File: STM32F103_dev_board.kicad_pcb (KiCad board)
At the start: 4 copper layers, 39.4 x 83.8 mm, 40 parts, among them IC2 FT232RNL-REEL, J1 Conn_ARM_JTAG_SWD_20, J2 Conn_01x20_Pin, J3 Conn_01x20_Pin, J6 USB4800-03-A, U1 STM32F103RBTx, Y1 8MHz, Y2 Crystal_GND23

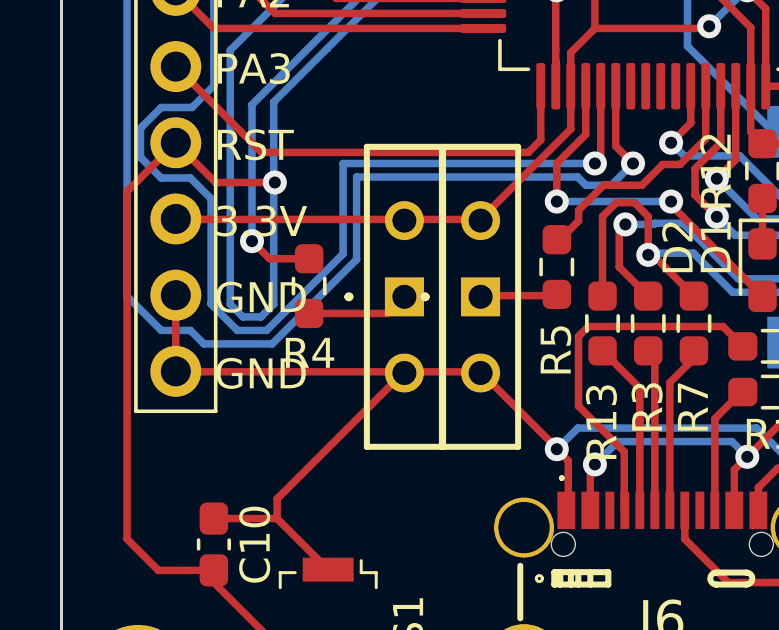
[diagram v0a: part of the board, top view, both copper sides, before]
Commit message: Moved R4 resistor position slightly
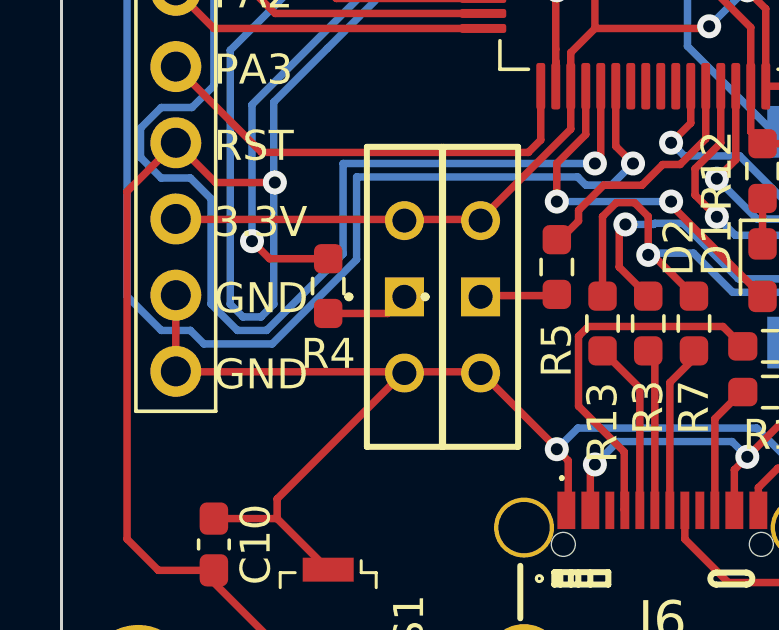
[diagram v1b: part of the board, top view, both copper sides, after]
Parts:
- moved R4 0.63 mm to (134.6, 126.0)
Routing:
- net Net-(S2-COM): track 3.40 -> 2.77 mm
- net BOOT0: track 26.2 -> 26.8 mm
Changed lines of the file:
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@@
   )
   (footprint "Resistor_SMD:R_0603_1608Metric_Pad0.98x0.95mm_HandSolder" (layer "F.Cu")
-    (at 133.985 126.0075 90)
+    (at 134.62 126.0075 90)
     (descr "Resistor SMD 0603 (1608 Metric), square (rectangular) end terminal, IPC_7351 nominal with elongated pad for handsoldering. (Body size source: IPC-SM-782 page 72, https://www.pcb-3d.com/wordpress/wp-content/uploads/ipc-sm-782a_amendment_1_and_2.pdf), generated with kicad-footprint-generator")
     (tags "resistor handsolder")
@@
   (segment (start 151.13 116.42) (end 161.02 116.42) (width 0.25) (layer "F.Cu") (net 41))
   (segment (start 161.02 116.42) (end 161.29 116.15) (width 0.25) (layer "F.Cu") (net 41))
-  (segment (start 133.985 126.92) (end 136.605 126.92) (width 0.25) (layer "F.Cu") (net 42))
+  (segment (start 134.62 126.92) (end 136.605 126.92) (width 0.25) (layer "F.Cu") (net 42))
   (segment (start 136.605 126.92) (end 137.16 126.365) (width 0.25) (layer "F.Cu") (net 42))
   (segment (start 144.488 133.462) (end 144.508 133.482) (width 0.25) (layer "F.Cu") (net 43))
@@
   (segment (start 161.776701 122.595) (end 162.465 123.283299) (width 0.25) (layer "B.Cu") (net 53))
   (segment (start 160.803299 122.595) (end 161.776701 122.595) (width 0.25) (layer "B.Cu") (net 53))
+  (segment (start 134.62 125.095) (end 132.6655 125.095) (width 0.25) (layer "F.Cu") (net 54))
   (segment (start 143.705 109.605) (end 143.51 109.8) (width 0.25) (layer "F.Cu") (net 54))
-  (segment (start 132.6655 125.095) (end 133.985 125.095) (width 0.25) (layer "F.Cu") (net 54))
   (segment (start 132.6655 125.095) (end 132.08 124.5095) (width 0.25) (layer "F.Cu") (net 54))
   (segment (start 143.705 107.995) (end 143.705 109.605) (width 0.25) (layer "F.Cu") (net 54))

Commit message: Minor changes
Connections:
- S2 pad 3: unconnected-(S2-NC-Pad3) -> VCC3V3
- S3 pad 3: unconnected-(S3-NC-Pad3) -> VCC3V3
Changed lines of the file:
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@@
   (net 89 "PB5")
   (net 90 "Net-(S3-COM)")
-  (net 91 "unconnected-(S2-NC-Pad3)")
-  (net 92 "unconnected-(S3-NC-Pad3)")
   (footprint "Capacitor_SMD:C_0603_1608Metric_Pad1.08x0.95mm_HandSolder" (layer "F.Cu")
     (at 152.72 130.12 180)
@@
       (net 78 "GND") (pinfunction "NO") (pintype "passive"))
     (pad "3" thru_hole circle (at -2.54 0 270) (size 1.3 1.3) (drill 0.8) (layers "*.Cu" "*.Mask")
-      (net 91 "unconnected-(S2-NC-Pad3)") (pinfunction "NC") (pintype "no_connect"))
-    (model "C:\\Lib\\SamacSys_Parts\\SamacSys_Parts.3dshapes\\BSI-10.stp"
+      (net 80 "VCC3V3") (pinfunction "NC") (pintype "passive"))
+    (model "C:\\lib\\samacsys\\SamacSys_Parts.3dshapes\\BSI-10.stp"
       (offset (xyz 0 0 0))
       (scale (xyz 1 1 1))
@@
     (pad "5" smd rect (at 1.25 -0.95 180) (size 0.6 1.2) (layers "F.Cu" "F.Paste" "F.Mask")
       (net 80 "VCC3V3") (pinfunction "OUT") (pintype "output"))
-    (model "C:\\Lib\\SamacSys_Parts\\SamacSys_Parts.3dshapes\\TLV75733PDBVR.stp"
+    (model "C:\\lib\\samacsys\\SamacSys_Parts.3dshapes\\TLV75733PDBVR.stp"
       (offset (xyz 0 0 0))
       (scale (xyz 1 1 1))
@@
       (net 78 "GND") (pinfunction "NO") (pintype "passive"))
     (pad "3" thru_hole circle (at -2.54 0 270) (size 1.3 1.3) (drill 0.8) (layers "*.Cu" "*.Mask")
-      (net 92 "unconnected-(S3-NC-Pad3)") (pinfunction "NC") (pintype "no_connect"))
-    (model "C:\\Lib\\SamacSys_Parts\\SamacSys_Parts.3dshapes\\BSI-10.stp"
+      (net 80 "VCC3V3") (pinfunction "NC") (pintype "passive"))
+    (model "C:\\lib\\samacsys\\SamacSys_Parts.3dshapes\\BSI-10.stp"
       (offset (xyz 0 0 0))
       (scale (xyz 1 1 1))
@@
     (pad "28" smd rect (at 3.512 4.225 180) (size 0.45 1.725) (layers "B.Cu" "B.Paste" "B.Mask")
       (net 76 "unconnected-(IC2-OSCO-Pad28)") (pinfunction "OSCO") (pintype "passive+no_connect"))
-    (model "C:\\Lib\\SamacSys_Parts\\SamacSys_Parts.3dshapes\\FT232RNL-TUBE.stp"
-      (offset (xyz 0 0 0))
-      (scale (xyz 1 1 1))
+    (model "C:\\lib\\samacsys\\SamacSys_Parts.3dshapes\\FT232RNL-REEL.stp"
+      (offset (xyz 0 0 0))
+      (scale (xyz 1 1 1))

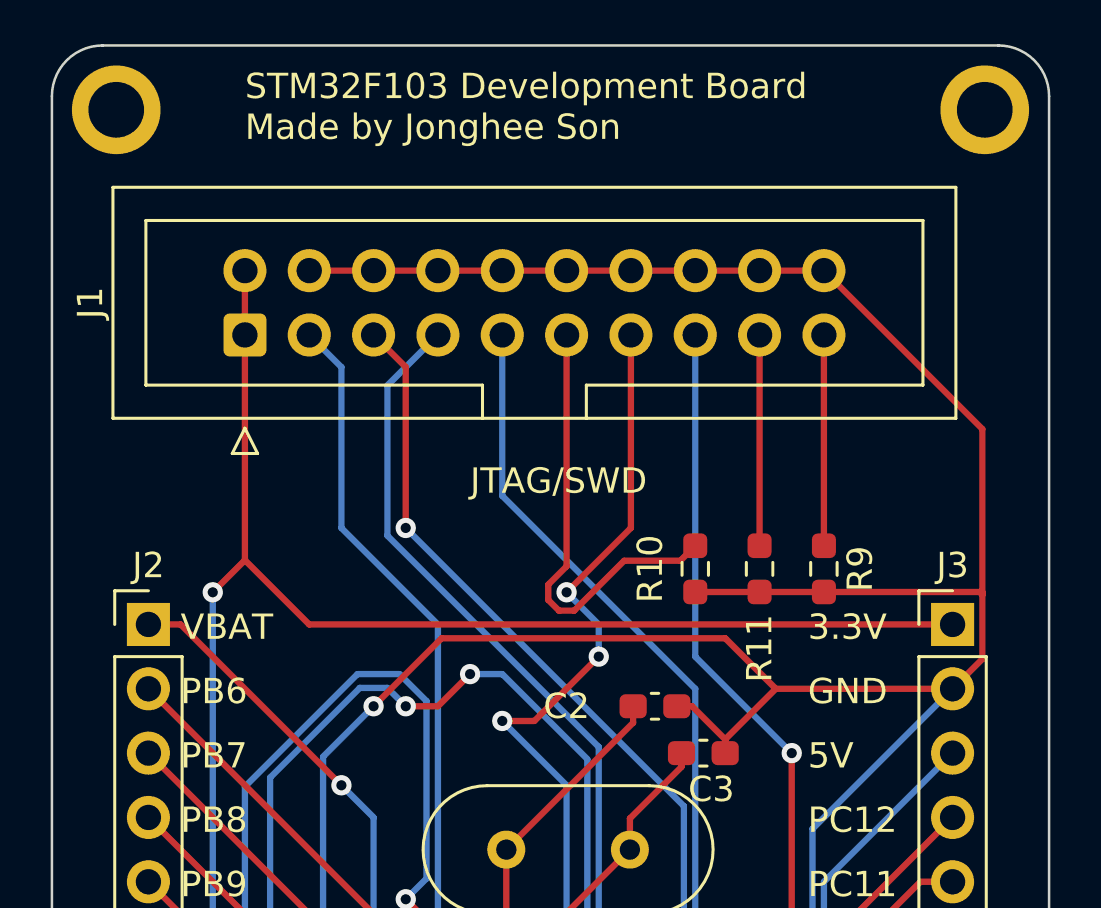
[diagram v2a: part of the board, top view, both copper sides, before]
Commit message: Changed direction of JTAG connector for easy connection
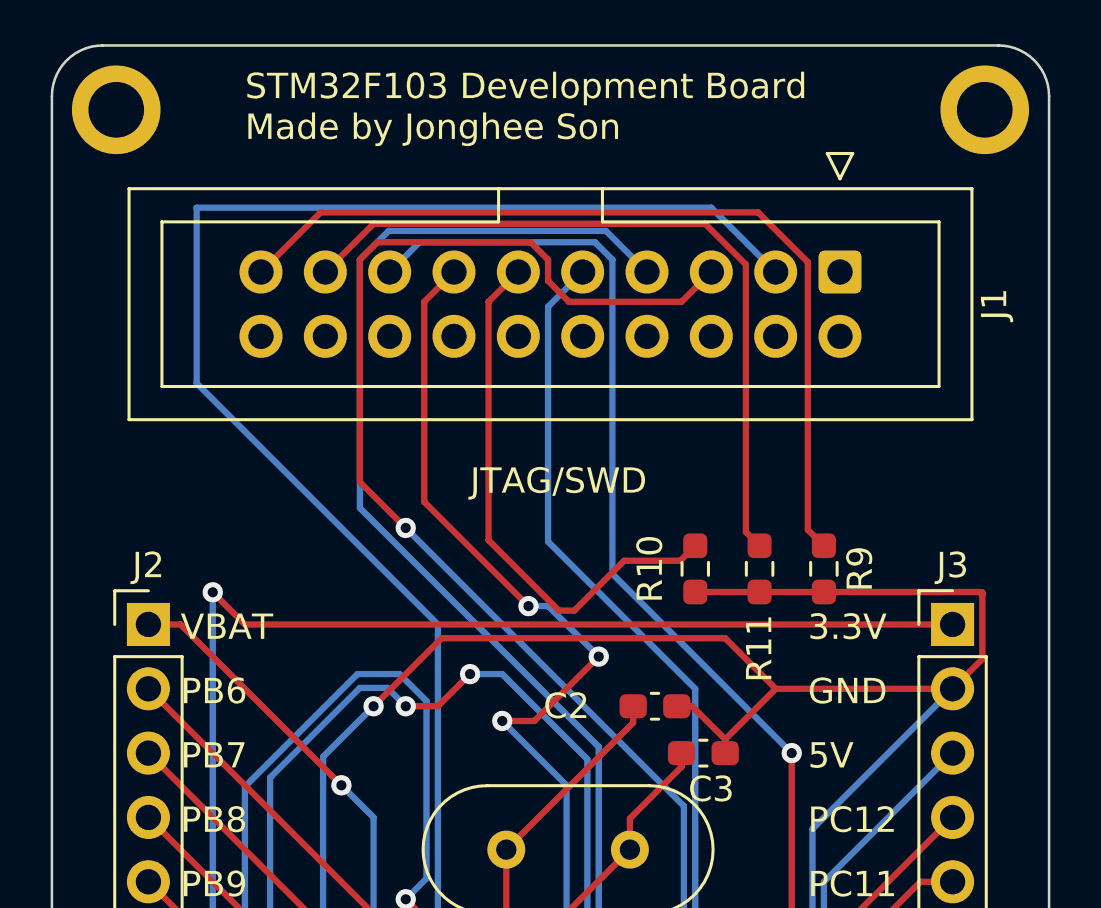
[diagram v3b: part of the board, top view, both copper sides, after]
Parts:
- moved J1 23.6 mm to (156.8, 66.7), turned to -90 degrees
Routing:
- net GND: track 306.2 -> 270.6 mm
- net JNTRST: track 42.9 -> 73.7 mm
- net Net-(J1-DBGACK/NC): track 8.32 -> 34.8 mm
- net Net-(J1-DBGRQ/NC): track 8.32 -> 29.4 mm
- net JTDI: track 44.7 -> 64.0 mm
- net JTMS/SWDIO: track 52.7 -> 67.8 mm
- net RESET: track 122.5 -> 136.4 mm
- net VCC3V3: track 147.3 -> 134.8 mm
- net JTDO: track 43.9 -> 48.6 mm
- net Net-(J1-RTCK): track 17.8 -> 21.4 mm
- net JTCK/SWCLK: track 42.8 -> 45.1 mm

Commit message: Added copper pour for 1st & 2nd layer
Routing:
- net VCC3V3: track 134.8 -> 66.4 mm, vias 5 -> 4
- added copper zone on B.Cu, net GND
- added copper zone on F.Cu, net GND
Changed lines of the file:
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@@
   (title_block
     (title "STM32F103RBT6 Dev Board")
-    (date "2023-12-15")
-    (rev "1.2.2")
+    (date "2023-12-16")
+    (rev "1.2.3")
   )
   (layers
@@
   (segment (start 150.43 109.22) (end 145.36 109.22) (width 0.25) (layer "F.Cu") (net 80))
   (segment (start 143.281695 110.769695) (end 143.51 110.998) (width 0.25) (layer "F.Cu") (net 80))
-  (segment (start 161.29 80.59) (end 133.35 80.59) (width 0.25) (layer "F.Cu") (net 80))
   (segment (start 152.405 124.841) (end 152.405 122.52) (width 0.25) (layer "F.Cu") (net 80))
   (segment (start 143.51 117.42) (end 143.51 113.030685) (width 0.25) (layer "F.Cu") (net 80))
   (segment (start 142.705 120.775) (end 139.695 123.785) (width 0.25) (layer "F.Cu") (net 80))
   (segment (start 142.705 118.225) (end 143.51 117.42) (width 0.25) (layer "F.Cu") (net 80))
-  (segment (start 133.35 80.59) (end 132.08 79.32) (width 0.25) (layer "F.Cu") (net 80))
   (segment (start 141.705 109.955) (end 142.095 110.345) (width 0.25) (layer "F.Cu") (net 80))
   (segment (start 143.51 114.88) (end 142.484695 114.88) (width 0.25) (layer "F.Cu") (net 80))
@@
   (segment (start 149.205 119.345) (end 150.911 119.345) (width 0.25) (layer "F.Cu") (net 80))
   (segment (start 149.205 116.765) (end 148.59 116.15) (width 0.25) (layer "F.Cu") (net 80))
-  (segment (start 132.08 79.32) (end 132.08 79.32) (width 0.25) (layer "F.Cu") (net 80))
   (segment (start 137.155 123.785) (end 129.555 123.785) (width 0.25) (layer "F.Cu") (net 80))
   (segment (start 151.13 109.92) (end 150.43 109.22) (width 0.25) (layer "F.Cu") (net 80))
@@
   (via (at 147.32 117.348) (size 0.8) (drill 0.4) (layers "F.Cu" "B.Cu") (net 80))
   (via (at 151.257 118.999) (size 0.8) (drill 0.4) (layers "F.Cu" "B.Cu") (net 80))
-  (via (at 132.08 79.32) (size 0.8) (drill 0.4) (layers "F.Cu" "B.Cu") (net 80))
   (via (at 143.51 110.998) (size 0.8) (drill 0.4) (layers "F.Cu" "B.Cu") (net 80))
   (segment (start 148.59 116.15) (end 148.518 116.15) (width 0.25) (layer "B.Cu") (net 80))
   (segment (start 147.32 117.42) (end 147.32 117.348) (width 0.25) (layer "B.Cu") (net 80))
   (segment (start 147.32 117.348) (end 147.392 117.348) (width 0.25) (layer "B.Cu") (net 80))
-  (segment (start 141.695 111.795) (end 132.08 102.18) (width 0.25) (layer "B.Cu") (net 80))
-  (segment (start 142.785 111.723) (end 143.51 110.998) (width 0.25) (layer "B.Cu") (net 80))
-  (segment (start 142.785 111.795) (end 141.695 111.795) (width 0.25) (layer "B.Cu") (net 80))
-  (segment (start 132.08 102.18) (end 132.08 79.32) (width 0.25) (layer "B.Cu") (net 80))
   (segment (start 147.32 117.42) (end 147.32 117.42) (width 0.25) (layer "B.Cu") (net 80))
   (segment (start 151.257 118.999) (end 151.42825 119.17025) (width 0.25) (layer "B.Cu") (net 80))
   (segment (start 148.518 116.15) (end 147.32 117.348) (width 0.25) (layer "B.Cu") (net 80))
   (segment (start 151.42825 119.17025) (end 151.42825 120.865) (width 0.25) (layer "B.Cu") (net 80))
-  (segment (start 142.785 111.795) (end 142.785 111.723) (width 0.25) (layer "B.Cu") (net 80))
   (segment (start 130.81 80.59) (end 129.54 80.59) (width 0.25) (layer "F.Cu") (net 81))
   (segment (start 138.43 107.26) (end 138.43 108.57) (width 0.25) (layer "F.Cu") (net 81))
@@
   (segment (start 139.71 126.31) (end 139.695 126.325) (width 0.25) (layer "F.Cu") (net 90))
   (segment (start 142.1765 126.325) (end 139.695 126.325) (width 0.25) (layer "F.Cu") (net 90))
+  (zone (net 78) (net_name "GND") (layer "F.Cu") (hatch edge 0.5)
+    (priority 2)
+    (connect_pads (clearance 0.5))
+    (min_thickness 0.25) (filled_areas_thickness no)
+    (fill yes (thermal_gap 0.5) (thermal_bridge_width 0.5))
+    (polygon
+      (pts
+        (xy 125.73 57.15)
+        (xy 165.1 57.15)
+        (xy 165.1 141.605)
+        (xy 125.73 141.605)
+      )
+    )
+  )
   (zone (net 80) (net_name "VCC3V3") (layer "In1.Cu") (hatch edge 0.5)
     (connect_pads (clearance 0.5))
@@
     (connect_pads (clearance 0.5))
     (min_thickness 0.25) (filled_areas_thickness no)
+    (fill yes (thermal_gap 0.5) (thermal_bridge_width 0.5))
+    (polygon
+      (pts
+        (xy 125.73 57.15)
+        (xy 165.1 57.15)
+        (xy 165.1 141.605)
+        (xy 125.73 141.605)
+      )
+    )
+  )
+  (zone (net 78) (net_name "GND") (layer "B.Cu") (hatch edge 0.5)
+    (priority 3)
+    (connect_pads (clearance 0.5))
+    (min_thickness 0.25) (filled_areas_thickness no)

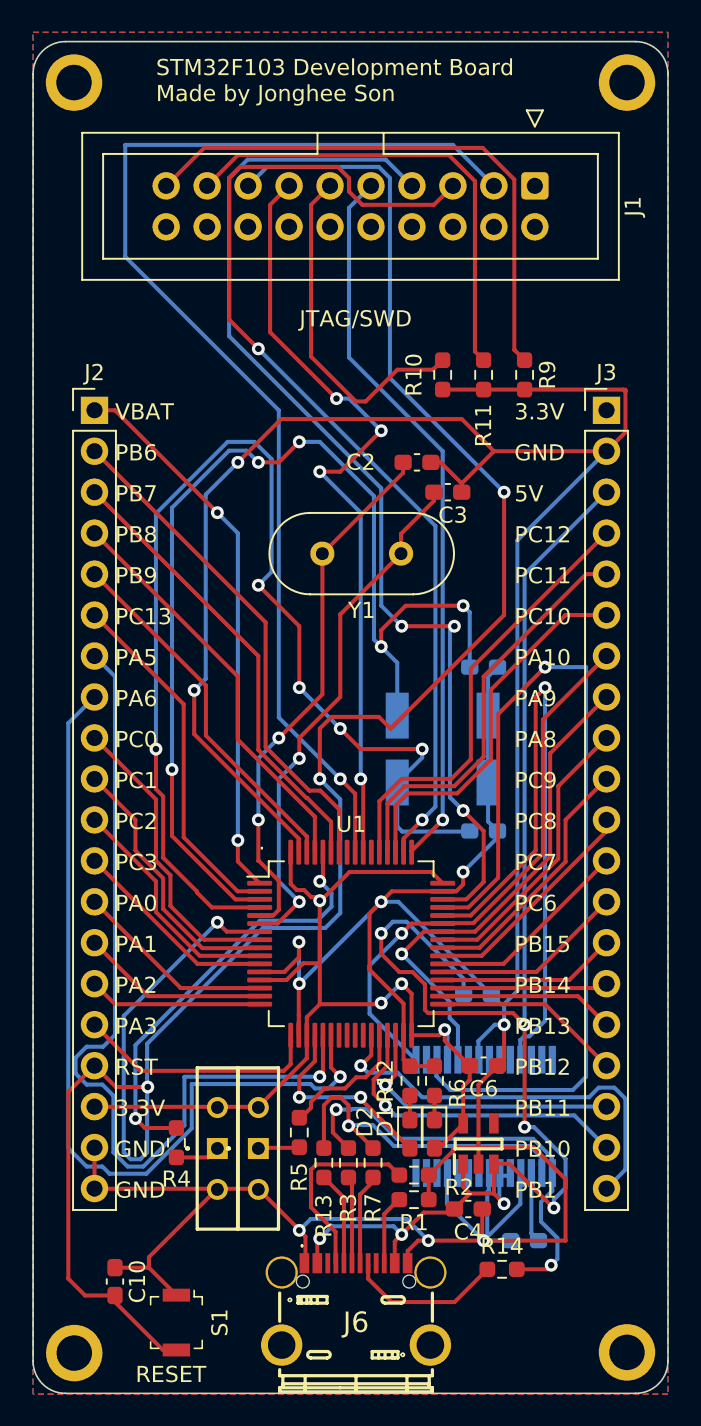
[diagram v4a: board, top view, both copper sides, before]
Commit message: Changed 8MHz oscillator to SMD one
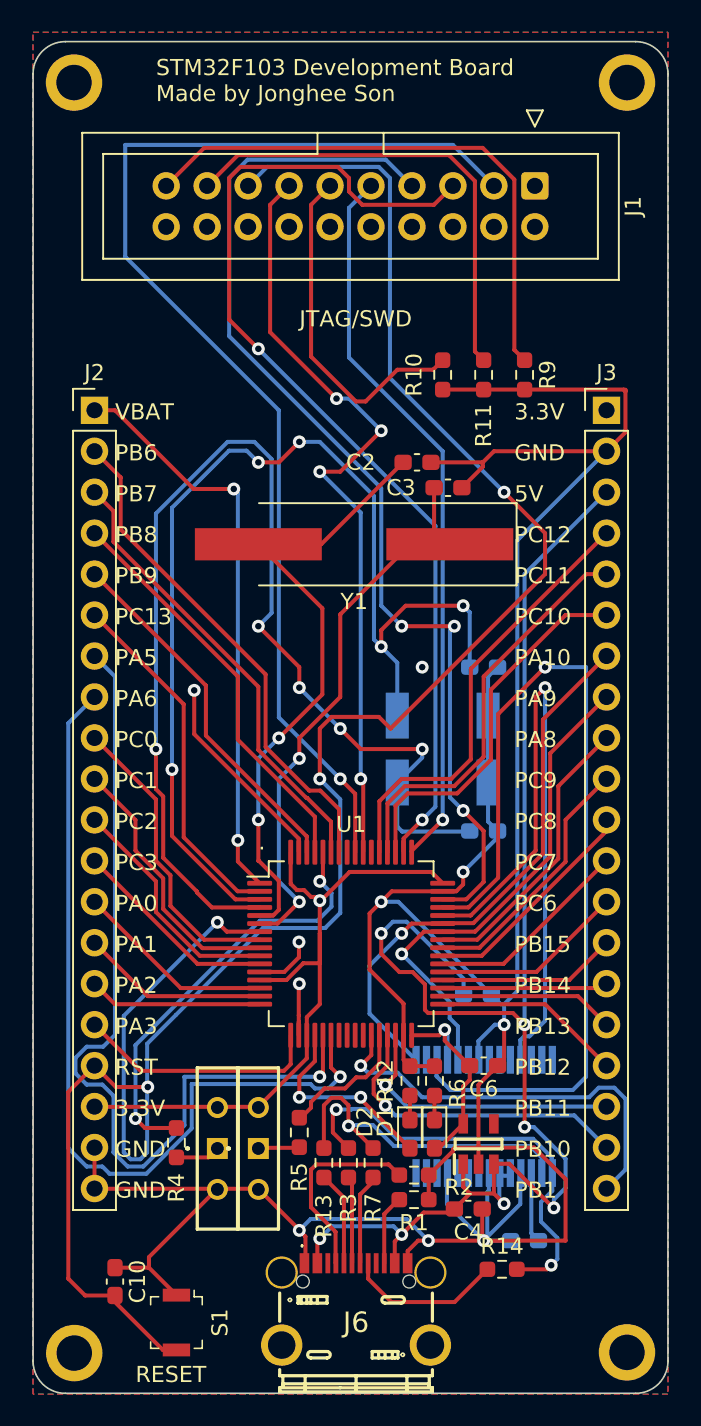
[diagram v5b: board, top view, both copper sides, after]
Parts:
- Y1: footprint Crystal:Crystal_HC49-4H_Vertical -> Crystal:Crystal_SMD_HC49-SD_HandSoldering
- moved Y1 2.97 mm to (145.6, 88.9)
- moved C3 0.28 mm to (151.5, 85.4)
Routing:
- net GND: track 270.6 -> 228.2 mm
- net VCC3V3: track 66.4 -> 57.2 mm, vias 4 -> 2
- net OSC_IN: track 33.3 -> 38.9 mm
- net OSC_OUT: track 32.9 -> 35.5 mm
- net RESET: track 136.4 -> 138.5 mm
- net VBAT: track 34.3 -> 35.8 mm
